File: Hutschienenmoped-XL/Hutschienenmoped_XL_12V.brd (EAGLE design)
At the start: 96.3 x 101.8 mm, 126 parts, among them J1 638207222005, J13 638207222005, J15 638207222008, J2 645004114822, J4 61300421121, J7 638207222005, J8 638207222007, U4 TLE9250VSJ

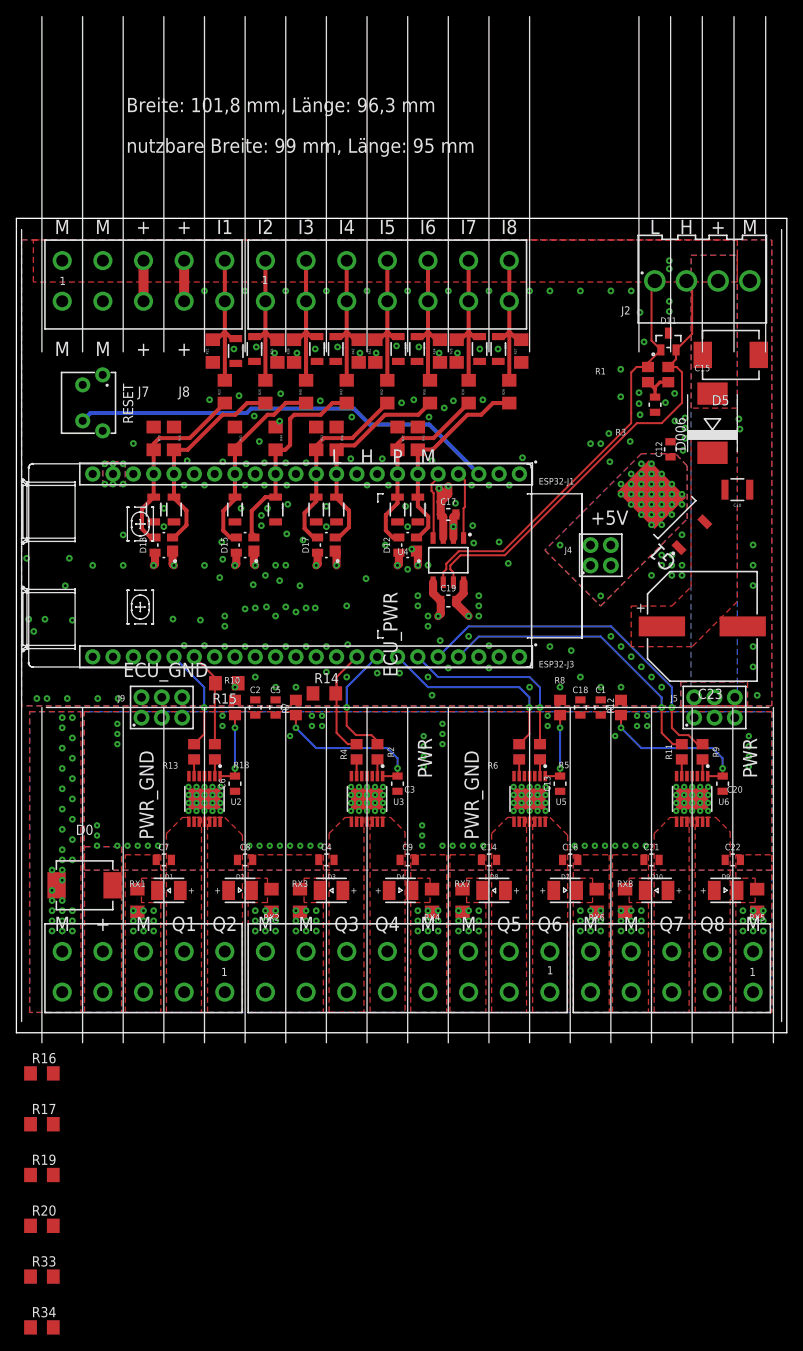
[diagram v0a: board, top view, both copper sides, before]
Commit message: Update grid distance and layer visibility settings, adjust resistor element positions and orientations.
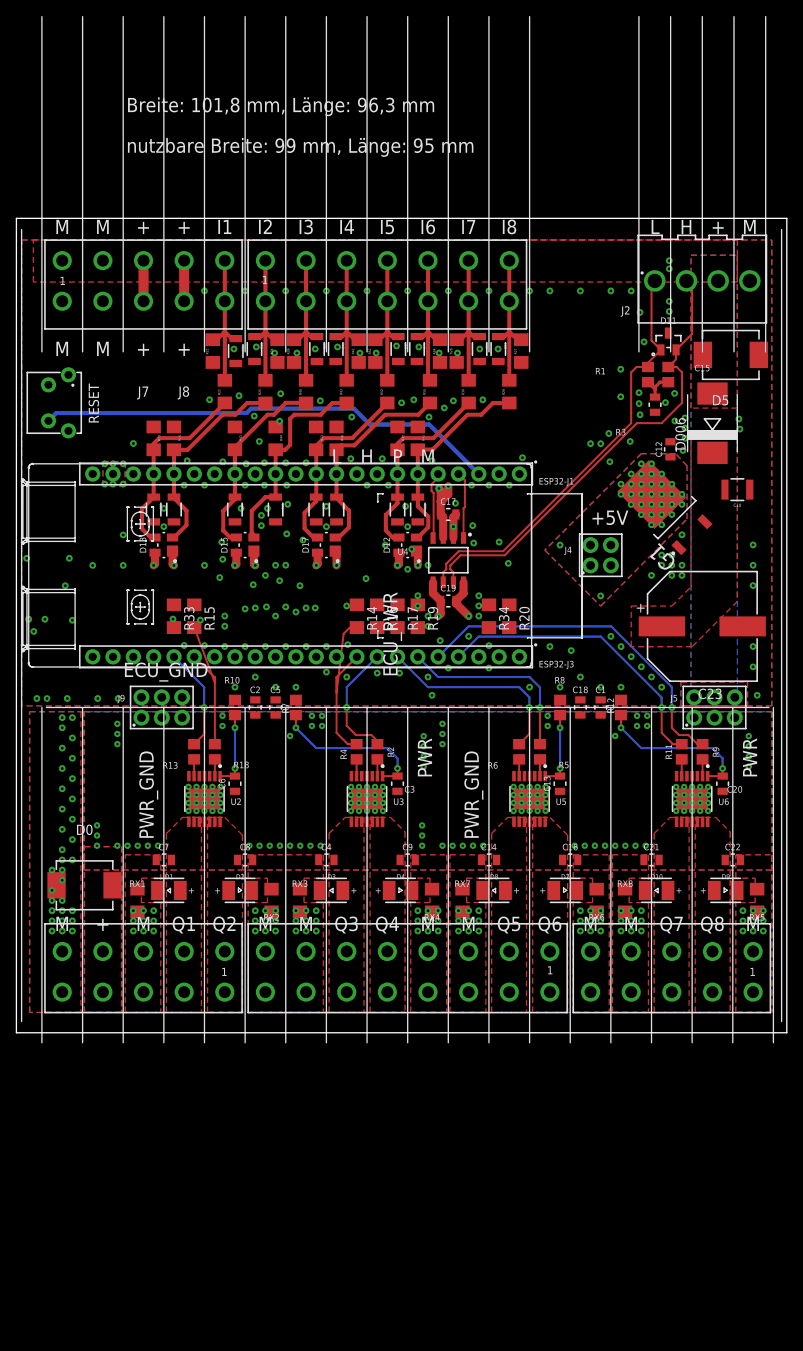
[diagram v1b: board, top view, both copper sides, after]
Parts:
- moved R34 105.0 mm to (58.4, 52.1), turned to 270 degrees
- moved R20 96.0 mm to (61.0, 52.1), turned to 270 degrees
- moved R19 84.2 mm to (49.5, 52.1), turned to 270 degrees
- moved R33 84.2 mm to (19.1, 52.1), turned to 270 degrees
- moved R17 77.5 mm to (47.0, 52.1), turned to 270 degrees
- moved R16 70.9 mm to (44.5, 52.1), turned to 270 degrees
- moved R14 10.5 mm to (41.9, 52.1), turned to 270 degrees
- moved R15 9.32 mm to (21.6, 52.1), turned to 270 degrees
- moved RESET 4.28 mm to (4.61, 78.7)
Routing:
- net Q3C: track 15.7 -> 24.1 mm
- net Q2C: track 12.8 -> 20.0 mm
- net RESET: track 53.5 -> 57.8 mm

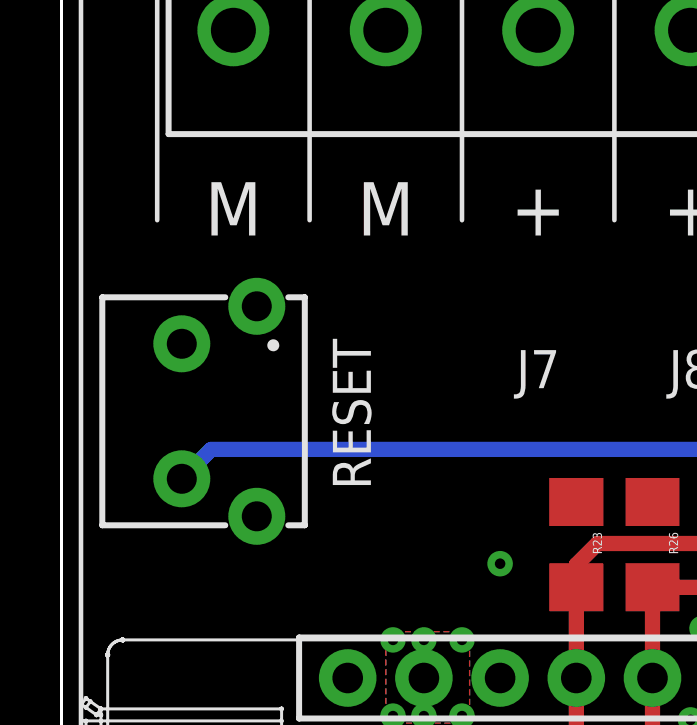
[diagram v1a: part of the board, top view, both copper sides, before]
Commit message: Add new board file with layer settings and circuit layout.
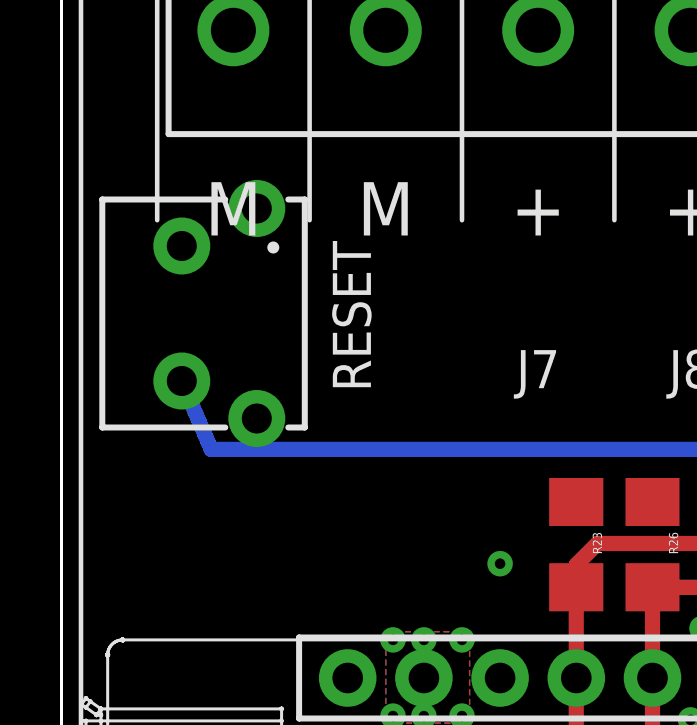
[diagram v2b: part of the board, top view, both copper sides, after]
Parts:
- moved RESET 3.26 mm to (4.61, 82.0)
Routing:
- net RESET: track 57.8 -> 58.9 mm
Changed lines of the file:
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@@
 </layers>
 <board>
-<fusionsync huburn="a.YnVzaW5lc3M6bXNtdWM" projecturn="a.YnVzaW5lc3M6bXNtdWMjMjAyMjAzMTc1MDgxMzE4ODE" f3durn="urn:adsk.wipprod:dm.lineage:AZr2ohsdTDeaNf8dmFIMlA" pcbguid="" lastpulledtime="" lastsyncedchangeguid="" latestrevisionid="3a181181-be39-4099-b846-b906128e2d27" lastsyncedrevisionid="3a181181-be39-4099-b846-b906128e2d27" lastboardhashguid="63f09d5a-3340-6f6f-8fc5-133538d7377f" lastpushedtime="2024-07-07T08:26:21Z" linktopcb3d="true"/>
+<fusionsync huburn="a.YnVzaW5lc3M6bXNtdWM" projecturn="a.YnVzaW5lc3M6bXNtdWMjMjAyMjAzMTc1MDgxMzE4ODE" f3durn="urn:adsk.wipprod:dm.lineage:AZr2ohsdTDeaNf8dmFIMlA" pcbguid="" lastpulledtime="" lastsyncedchangeguid="" latestrevisionid="25d4beac-188d-4e0d-9dc1-4fed8a35951d" lastsyncedrevisionid="25d4beac-188d-4e0d-9dc1-4fed8a35951d" lastboardhashguid="84b5fabf-717a-1f2a-69b5-34e3e12fd72e" lastpushedtime="2024-07-16T14:49:39Z" linktopcb3d="true"/>
 <plain>
 <wire x1="52.04" y1="41.46" x2="50.54" y2="41.46" width="0.1524" layer="22"/>
@@
 <attribute name="VALUE" x="55.88" y="53.34" size="1.27" layer="27" rot="R270"/>
 </element>
-<element name="RESET" library="Wurth_Switch_WS-TATU" library_urn="urn:adsk.eagle:library:18255789" package="4312560837X6" package3d_urn="urn:adsk.eagle:package:18255800/2" value="" x="4.61" y="78.74" smashed="yes" rot="R270">
-<attribute name="DATASHEET-URL" value="https://www.we-online.com/catalog/datasheet/431256083736.pdf" x="4.61" y="78.74" size="1.778" layer="27" rot="R270" display="off"/>
-<attribute name="H" value="8.35mm" x="4.61" y="78.74" size="1.778" layer="27" rot="R270" display="off"/>
-<attribute name="NAME" x="8.3941" y="78.64" size="1.27" layer="25" rot="R270" align="bottom-center"/>
-<attribute name="OPERATION-FORCE" value="360g" x="4.61" y="78.74" size="1.778" layer="27" rot="R270" display="off"/>
-<attribute name="PART-NUMBER" value="431256083736" x="4.61" y="78.74" size="1.778" layer="27" rot="R270" display="off"/>
-<attribute name="QTY" value=" 500 " x="4.61" y="78.74" size="1.778" layer="27" rot="R270" display="off"/>
-<attribute name="VALUE" x="-1.3322" y="76.41" size="1.27" layer="27" rot="R270"/>
+<element name="RESET" library="Wurth_Switch_WS-TATU" library_urn="urn:adsk.eagle:library:18255789" package="4312560837X6" package3d_urn="urn:adsk.eagle:package:18255800/2" value="" x="4.61" y="82" smashed="yes" rot="R270">
+<attribute name="DATASHEET-URL" value="https://www.we-online.com/catalog/datasheet/431256083736.pdf" x="4.61" y="82" size="1.778" layer="27" rot="R270" display="off"/>
+<attribute name="H" value="8.35mm" x="4.61" y="82" size="1.778" layer="27" rot="R270" display="off"/>
+<attribute name="NAME" x="8.3941" y="81.9" size="1.27" layer="25" rot="R270" align="bottom-center"/>
+<attribute name="OPERATION-FORCE" value="360g" x="4.61" y="82" size="1.778" layer="27" rot="R270" display="off"/>
+<attribute name="PART-NUMBER" value="431256083736" x="4.61" y="82" size="1.778" layer="27" rot="R270" display="off"/>
+<attribute name="QTY" value=" 500 " x="4.61" y="82" size="1.778" layer="27" rot="R270" display="off"/>
+<attribute name="VALUE" x="-1.3322" y="79.67" size="1.27" layer="27" rot="R270"/>
 </element>
 </elements>
@@
 <contactref element="ESP32-J3" pad="18"/>
 <contactref element="R33" pad="2"/>
-<wire x1="19.05" y1="50.648" x2="21.56" y2="36.0728" width="0" layer="19" extent="1-1"/>
+<wire x1="19.05" y1="46.99" x2="19.05" y2="50.648" width="0" layer="19" extent="1-1"/>
 </signal>
 <signal name="Q2C">
@@
 <contactref element="ESP32-J3" pad="8"/>
 <contactref element="R16" pad="2"/>
-<wire x1="44.45" y1="50.648" x2="44.48" y2="36.0728" width="0" layer="19" extent="1-1"/>
+<wire x1="44.45" y1="46.99" x2="44.45" y2="50.648" width="0" layer="19" extent="1-1"/>
 </signal>
 <signal name="Q3C">
@@
 <wire x1="40.259" y1="49.886" x2="39.37" y2="42.52" width="0.25" layer="1"/>
 <wire x1="39.37" y1="42.52" x2="39.37" y2="44.45" width="0.25" layer="1"/>
+<wire x1="41.021" y1="50.648" x2="41.91" y2="50.648" width="0" layer="19" extent="1-1"/>
 </signal>
 <signal name="ECU_PWR">
@@
 <contactref element="RESET" pad="1"/>
 <contactref element="RESET" pad="2"/>
-<wire x1="32.258" y1="76.454" x2="31.75" y2="75.717" width="0" layer="19" extent="1-1"/>
-<wire x1="46.99" y1="63.855" x2="48.26" y2="63.266" width="0" layer="19" extent="1-1"/>
-<wire x1="44.45" y1="53.492" x2="1.905" y2="41.783" width="0" layer="19" extent="1-1"/>
-<wire x1="46.99" y1="53.492" x2="44.45" y2="53.492" width="0" layer="19" extent="1-1"/>
-<wire x1="49.53" y1="53.492" x2="46.99" y2="53.492" width="0" layer="19" extent="1-1"/>
-<wire x1="60.96" y1="53.492" x2="49.53" y2="53.492" width="0" layer="19" extent="1-1"/>
-<wire x1="19.05" y1="53.492" x2="60.96" y2="53.492" width="0" layer="19" extent="1-1"/>
-<wire x1="58.42" y1="53.492" x2="19.05" y2="53.492" width="0" layer="19" extent="1-1"/>
 </signal>
 <signal name="BOOT">
@@
 <contactref element="ESP32-J1" pad="3"/>
 <contactref element="RESET" pad="3"/>
-<wire x1="3.36" y1="76.49" x2="4.34" y2="77.47" width="0.508" layer="16"/>
+<wire x1="3.36" y1="79.75" x2="4.34" y2="77.47" width="0.508" layer="16"/>
 <wire x1="50.967" y1="76.033" x2="57.15" y2="69.85" width="0.508" layer="16"/>
 <wire x1="28.15019375" y1="77.47" x2="28.69819375" y2="78.018" width="0.508" layer="16"/>
@@
 <contactref element="ESP32-J3" pad="7"/>
 <contactref element="R17" pad="2"/>
-<wire x1="46.99" y1="50.648" x2="46.99" y2="46.99" width="0" layer="19" extent="1-1"/>
+<wire x1="46.99" y1="46.99" x2="46.99" y2="50.648" width="0" layer="19" extent="1-1"/>
 </signal>
 <signal name="Q6C">
@@
 <contactref element="ESP32-J3" pad="6"/>
 <contactref element="R19" pad="2"/>
-<wire x1="49.53" y1="50.648" x2="49.53" y2="46.99" width="0" layer="19" extent="1-1"/>
+<wire x1="49.53" y1="46.99" x2="49.53" y2="50.648" width="0" layer="19" extent="1-1"/>
 </signal>
 <signal name="N$5">
@@
 <contactref element="ESP32-J3" pad="5"/>
 <contactref element="R34" pad="2"/>
-<wire x1="58.42" y1="50.648" x2="52.07" y2="46.99" width="0" layer="19" extent="1-1"/>
+<wire x1="52.07" y1="46.99" x2="58.42" y2="50.648" width="0" layer="19" extent="1-1"/>
 </signal>
 <signal name="Q7C">
@@
 <contactref element="ESP32-J3" pad="4"/>
 <contactref element="R20" pad="2"/>
-<wire x1="60.96" y1="50.648" x2="54.61" y2="46.99" width="0" layer="19" extent="1-1"/>
+<wire x1="54.61" y1="46.99" x2="60.96" y2="50.648" width="0" layer="19" extent="1-1"/>
 </signal>
 <signal name="N$15" class="1">
